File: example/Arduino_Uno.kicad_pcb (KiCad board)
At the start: 2 copper layers, 68.6 x 53.3 mm, 8 parts, among them J1 Power, J2 Digital/PWM, J3 Analog, J4 Digital/PWM

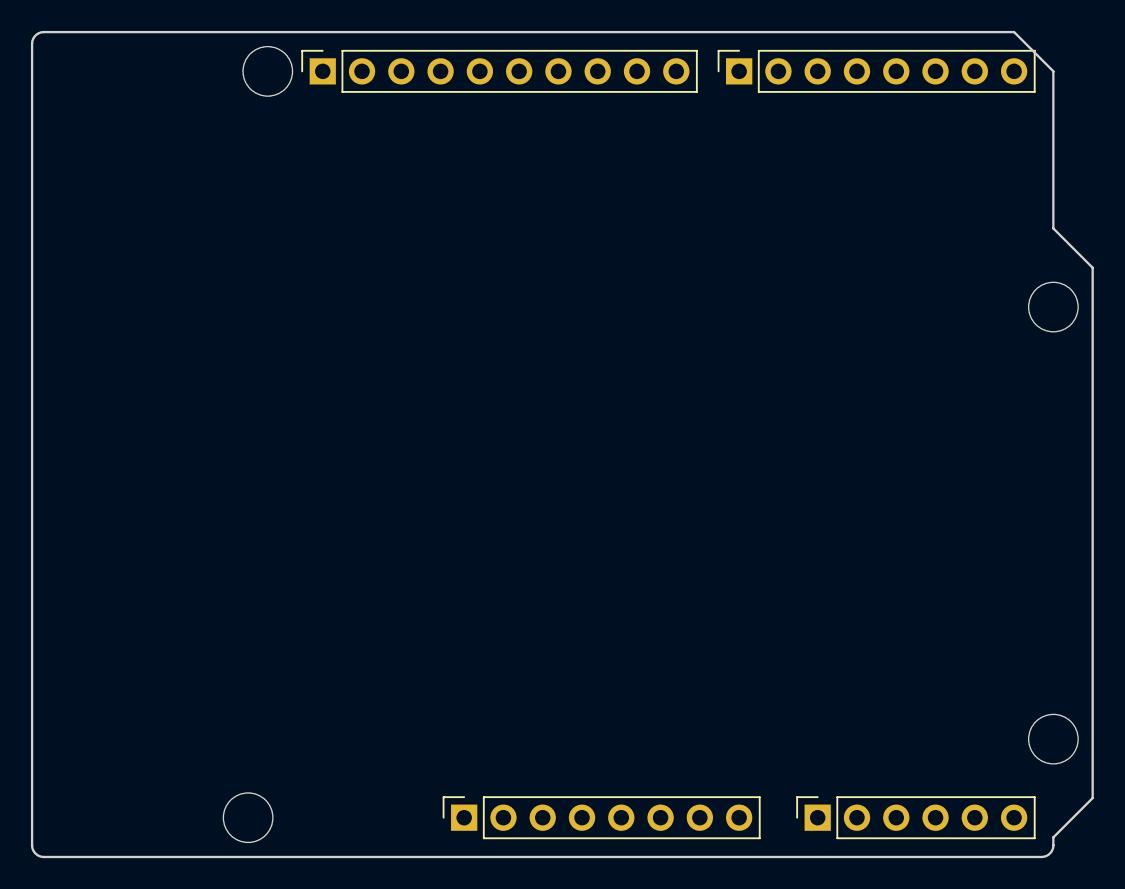
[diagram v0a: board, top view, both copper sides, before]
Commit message: Add SSD1306 OLED display to example (test diff feature)
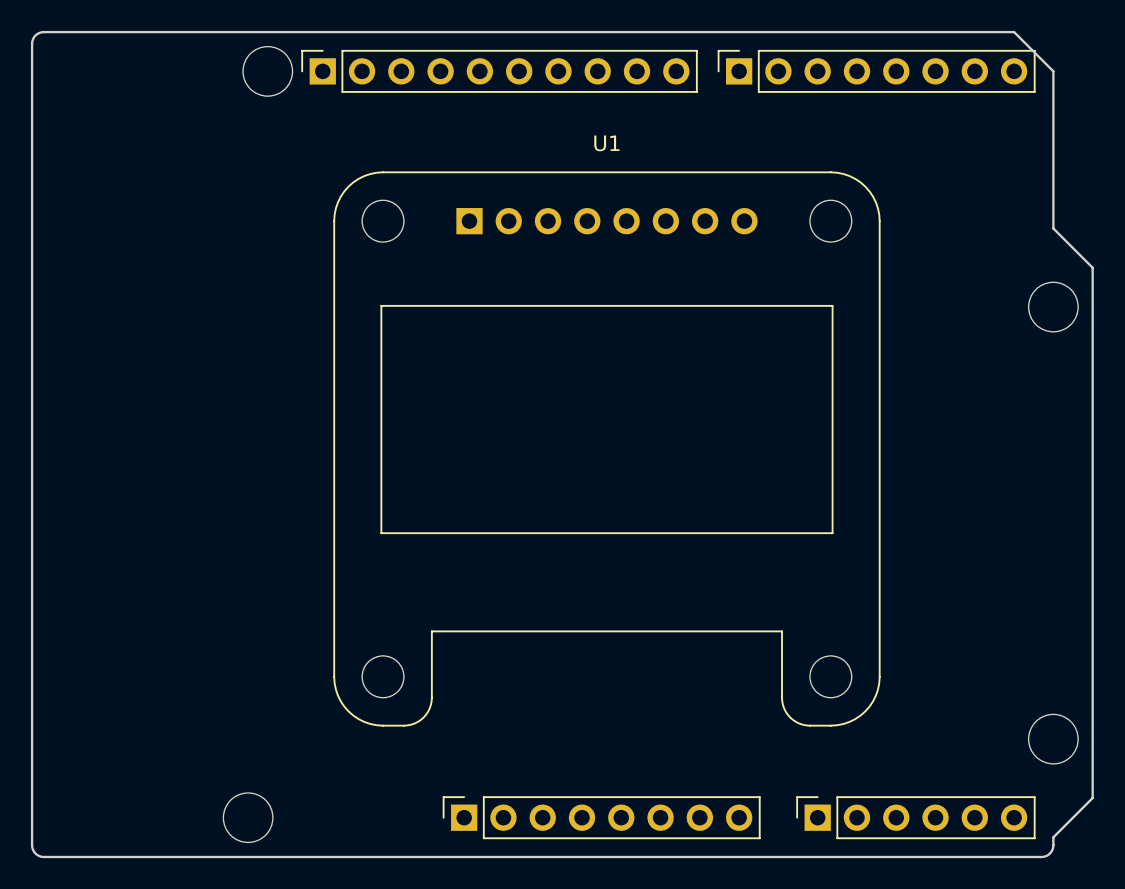
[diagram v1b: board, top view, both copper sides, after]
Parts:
- added U1: NHD-0420H1Z, Display:Adafruit_SSD1306, F.Cu at (128.3, 58.9)
